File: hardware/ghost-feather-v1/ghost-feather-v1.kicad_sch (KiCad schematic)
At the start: 66 parts, among them J1 Conn_ARM_SWD_TagConnect_TC2030, J2 USB_C_Receptacle_USB2.0, J3 Conn_01x03, J4 Conn_01x03, J5 Conn_01x03, J6 Conn_01x03, J7 Conn_01x08, Q1 BSS138, Q2 BSS138, Q3 BSS138, Q4 BSS138, SW2 BOOT0, U1 STM32F722RETx, U2 BMI270, U3 USBLC6-2SC6_MOD, U4 LM2596S-5, U5 ADP2108AUJ-3.3, X1 16MHz, X2 32kHz768

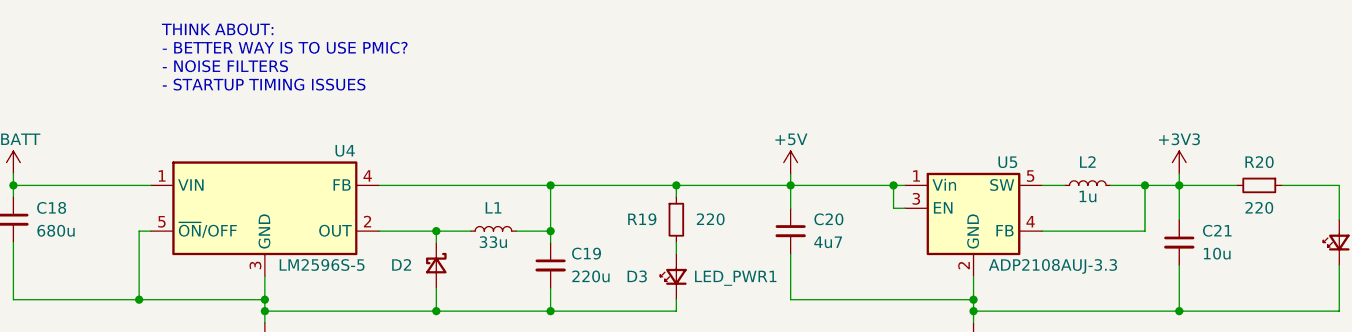
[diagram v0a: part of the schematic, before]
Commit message: feat: Add switching regulators related note
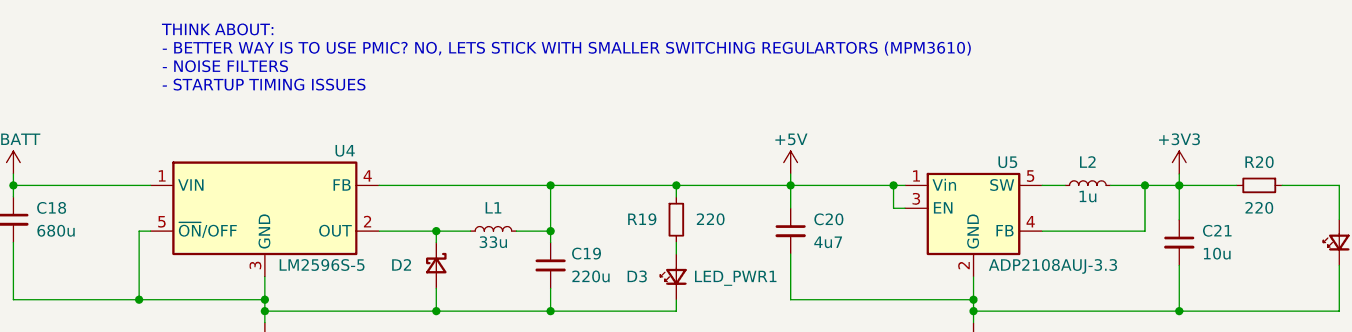
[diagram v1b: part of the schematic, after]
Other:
- note added: "THINK ABOUT: - BETTER WAY IS TO USE PMIC? NO, LETS STICK WITH SMALLER SWITCHING REGULARTORS (MPM3610) - NOISE FILTERS - STARTUP TIMING ISSUES"
- note removed: "THINK ABOUT: - BETTER WAY IS TO USE PMIC? - NOISE FILTERS - STARTUP TIMING ISSUES"
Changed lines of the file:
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@@
     (stroke (width 0) (type default))
   )
-  (text "THINK ABOUT:\n- BETTER WAY IS TO USE PMIC?\n- NOISE FILTERS\n- STARTUP TIMING ISSUES"
+  (text "THINK ABOUT:\n- BETTER WAY IS TO USE PMIC? NO, LETS STICK WITH SMALLER SWITCHING REGULARTORS (MPM3610)\n- NOISE FILTERS\n- STARTUP TIMING ISSUES"
     (at 100.33 44.45 0)
     (effects (font (size 1.27 1.27)) (justify left bottom))

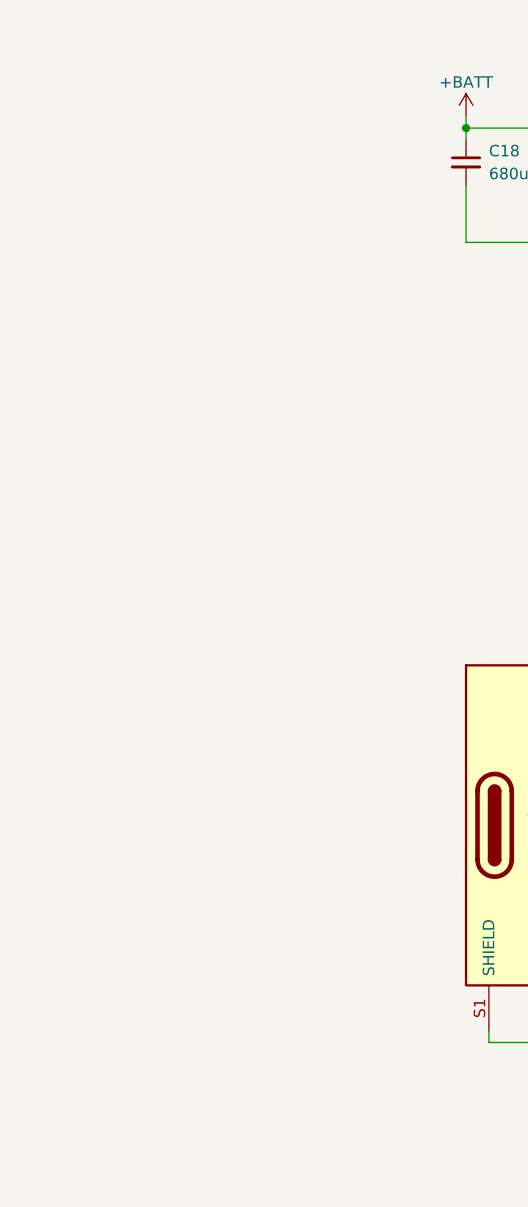
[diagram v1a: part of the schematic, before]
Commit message: feat: Add basic version of MPM3610 symbol
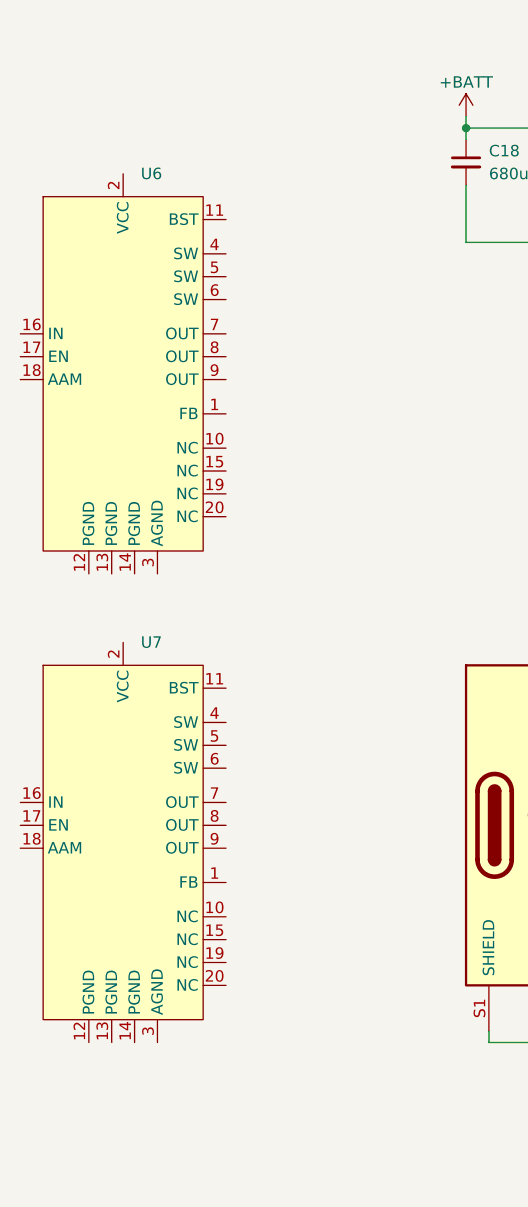
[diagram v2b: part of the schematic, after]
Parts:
- added U6, U7: ~, symbol ghost-feather-v1:MPM3610

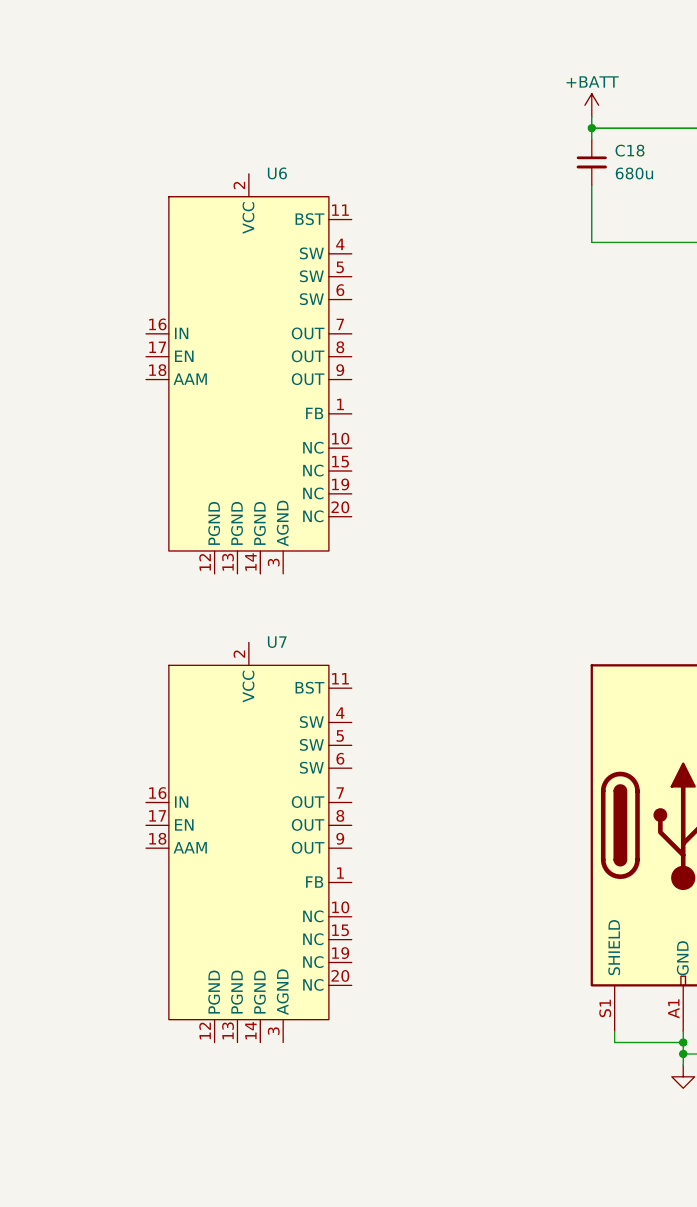
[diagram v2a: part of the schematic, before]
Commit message: feat: Add final version of MPM3610 symbol
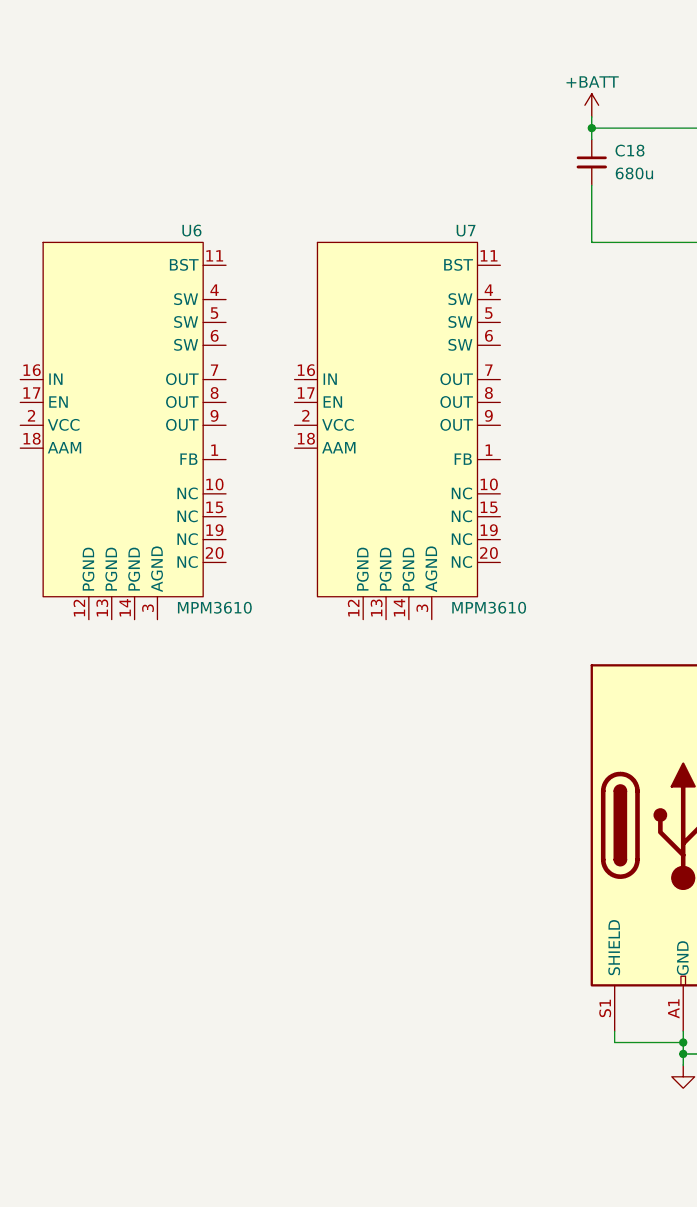
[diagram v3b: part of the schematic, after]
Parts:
- U6, U7: value ~ -> MPM3610

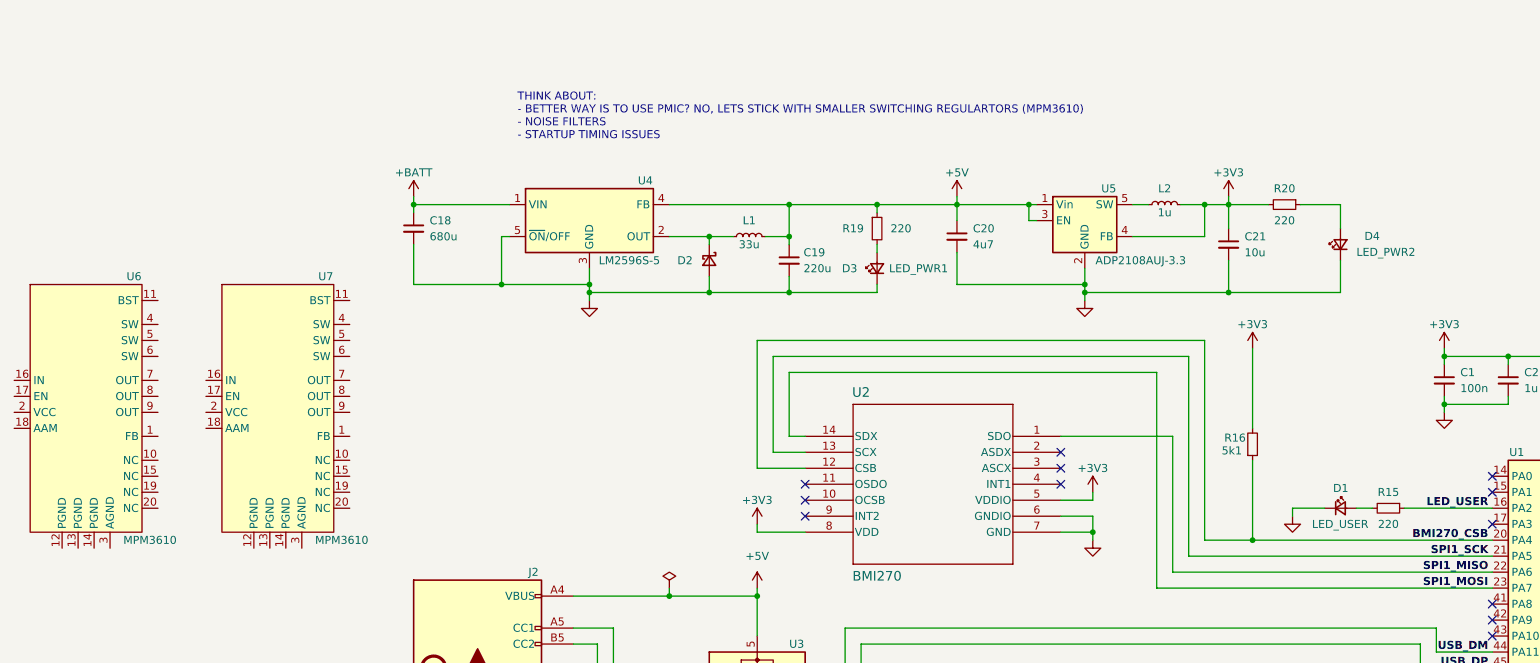
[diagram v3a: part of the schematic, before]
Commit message: cleanup: Delete previous switching regulators (too big)
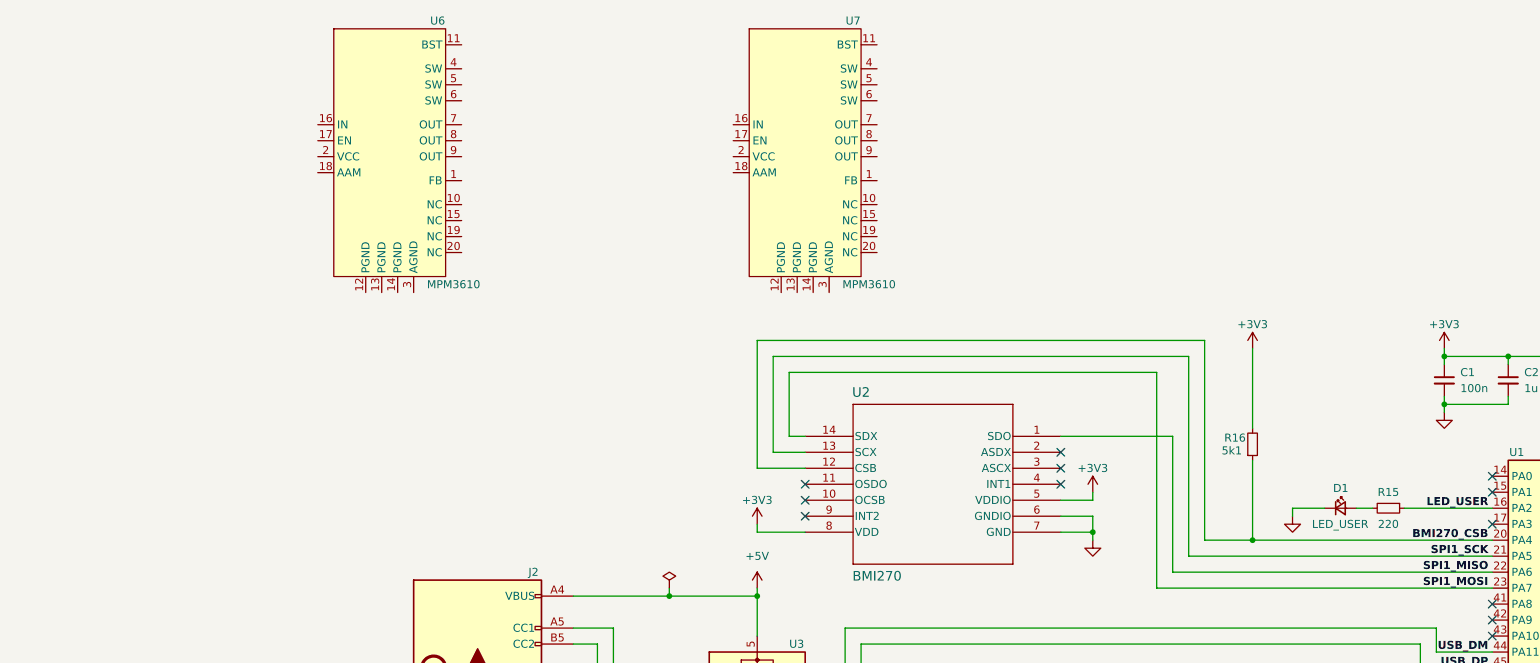
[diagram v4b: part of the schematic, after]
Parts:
- removed C18: 680u, ghost-feather-v1:CAPAE1350X1400N, symbol Device:C_Small
- removed C19: 220u, Capacitor_SMD:C_Elec_10x10.2, symbol Device:C_Small
- removed C20: 4u7, Capacitor_SMD:C_0603_1608Metric, symbol Device:C_Small
- removed C21: 10u, Capacitor_SMD:C_0603_1608Metric, symbol Device:C_Small
- removed D2: D_Schottky_Small, Diode_SMD:D_SMA, symbol Device:D_Schottky_Small
- removed D3: LED_PWR1, LED_SMD:LED_0402_1005Metric, symbol Device:LED_Small
- removed D4: LED_PWR2, LED_SMD:LED_0402_1005Metric, symbol Device:LED_Small
- removed L1: 33u, Inductor_SMD:L_12x12mm_H8mm, symbol Device:L_Small
- removed L2: 1u, Inductor_SMD:L_0805_2012Metric, symbol Device:L_Small
- removed R19, R20: 220, Resistor_SMD:R_0402_1005Metric, symbol Device:R_Small
- removed U4: LM2596S-5, Package_TO_SOT_SMD:TO-263-5_TabPin3, symbol Regulator_Switching:LM2596S-5
- removed U5: ADP2108AUJ-3.3, Package_TO_SOT_SMD:TSOT-23-5, symbol Regulator_Switching:ADP2108AUJ-3.3
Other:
- note removed: "THINK ABOUT: - BETTER WAY IS TO USE PMIC? NO, LETS STICK WITH SMALLER SWITCHING REGULARTORS (MPM3610) - NOISE FILTERS - STARTUP TIMING ISSUES"
- moved on the sheet: U6, U7

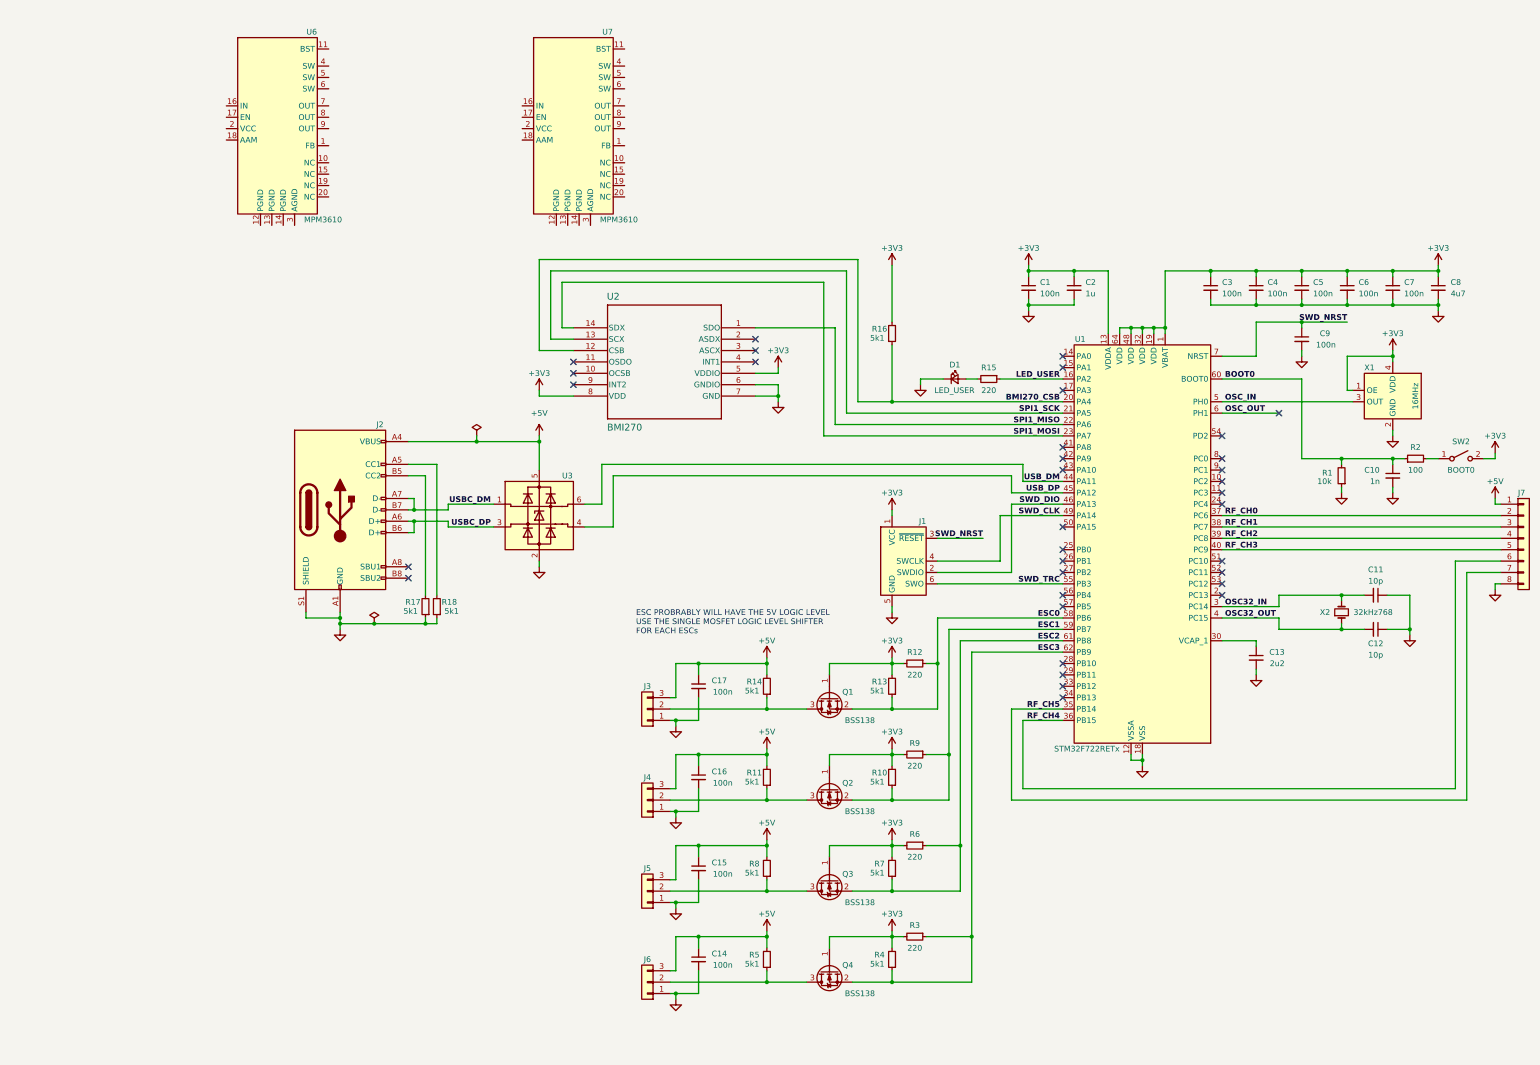
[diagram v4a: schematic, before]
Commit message: feat: Add the MPM3610 switching regulators #1
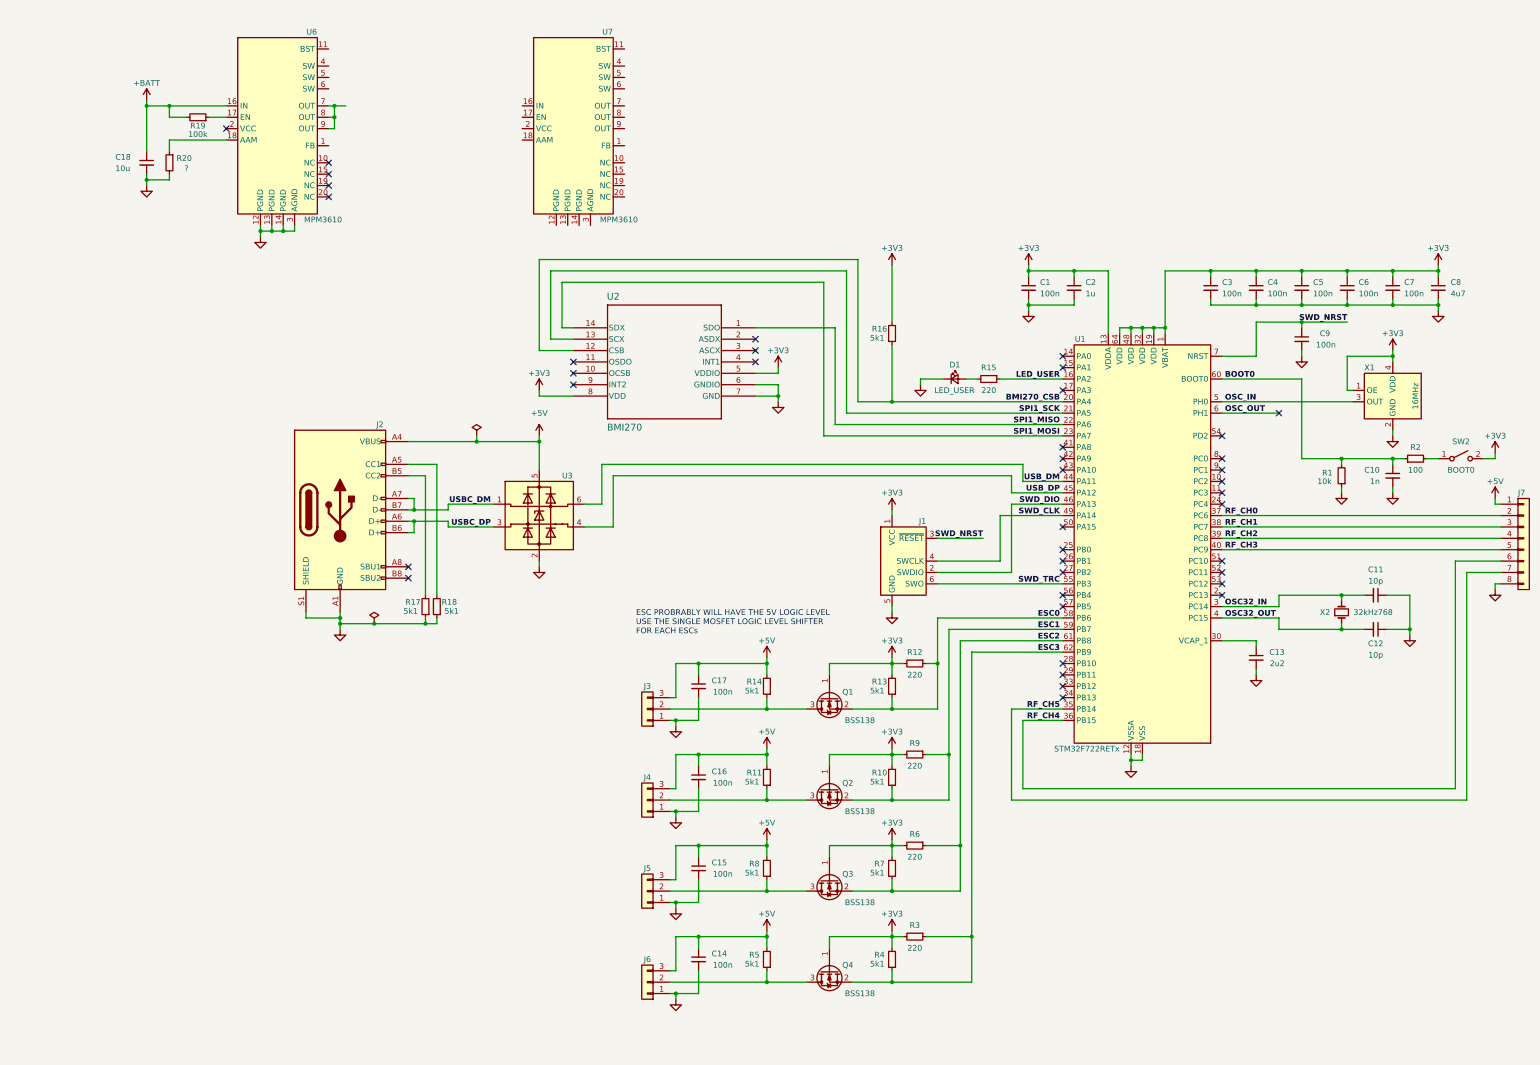
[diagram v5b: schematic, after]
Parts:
- added C18: 10u, Capacitor_SMD:C_0603_1608Metric, symbol Device:C_Small
- added R19: 100k, Resistor_SMD:R_0402_1005Metric, symbol Device:R_Small
- added R20: ?, Resistor_SMD:R_0402_1005Metric, symbol Device:R_Small
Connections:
- net GND: now also U6.12 (PGND), U6.13 (PGND), U6.14 (PGND), U6.3 (AGND), C18.2, R20.2
- net +BATT: now reaches U6.16 (IN)
- net +BATT: now also C18.1, R19.2
- net at U6.17 (EN): now also R19.1
- net at U6.18 (AAM): now also R20.1
- net at U6.7 (OUT): now also U6.8 (OUT), U6.9 (OUT)
- no-connect marks 35 -> 40
